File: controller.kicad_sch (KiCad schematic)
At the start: 42 parts, among them J1 Jumper_3_Bridged12, J2 EEPROM DISABLE, J3 Conn_02x20_Odd_Even, J4 5V, J5 USB_B_Mini, J6 Conn_01x05, J7 Jumper_3_Bridged12, SW2 RST, U1 CY7C68013A-56PVX, U2 AZ1117-3.3, U3 CAT24C128, Y1 24MHz

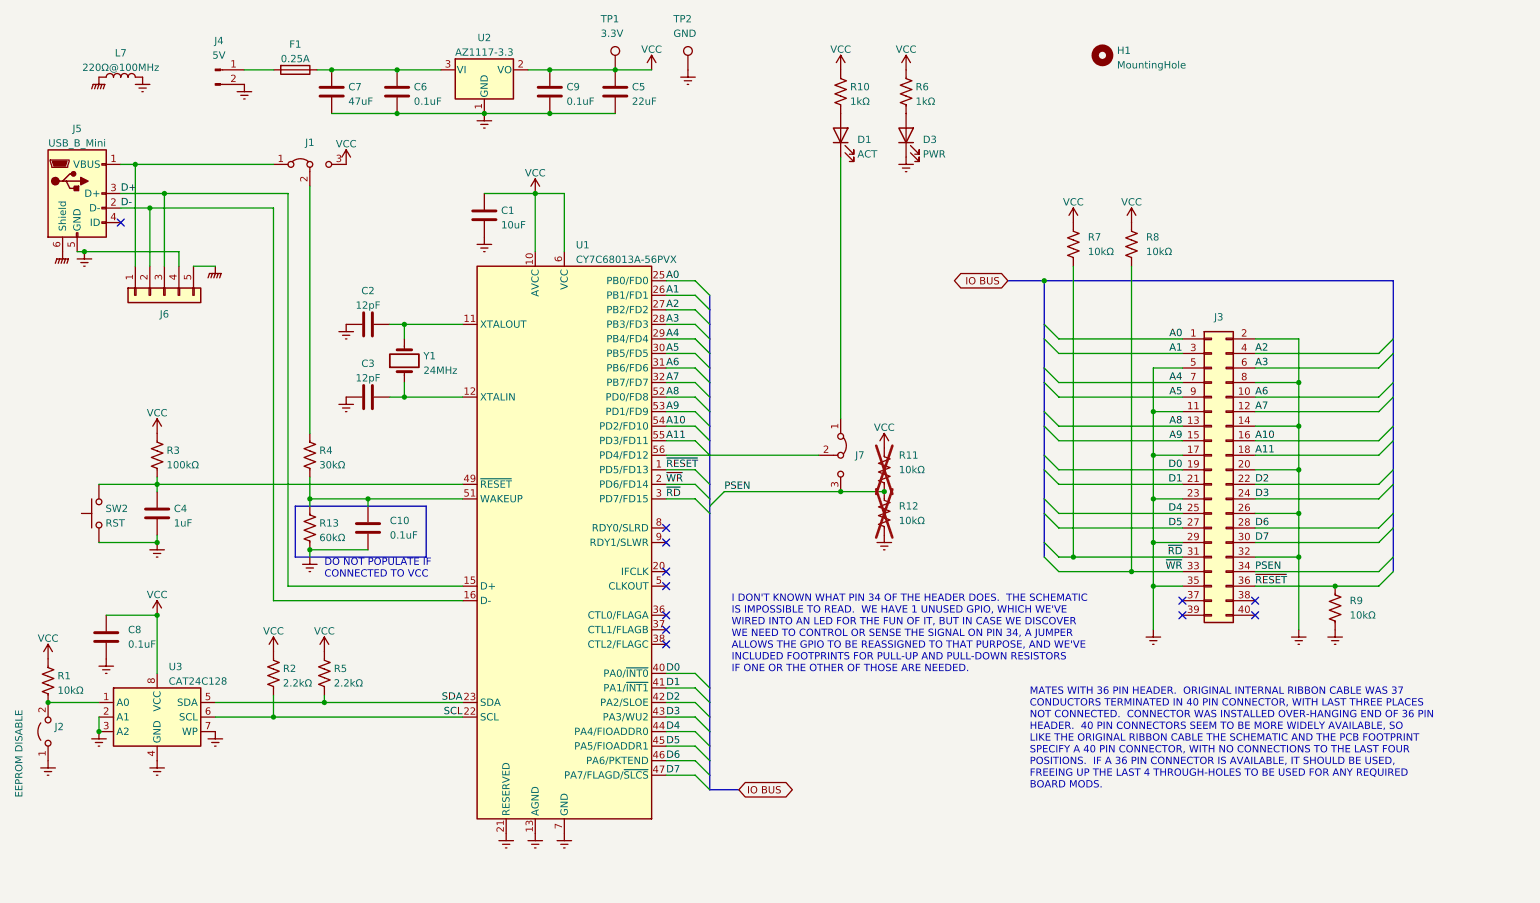
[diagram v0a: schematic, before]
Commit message: let's call this "version 2"
- this is a cleaned-up version of the board that was built and installed in the programmer
- the WAKEUP drain resistor & timing capacitor are included
- the board is hard-wired into the self-powered configuration (USB VBUS only used for WAKEUP)
- power delivery to the FX2 chip is (probably) improved
- the ground plane has fewer interruptions
- (almost) all spare pads and through-holes to accommodate possible mistakes are removed because they're known to not be needed
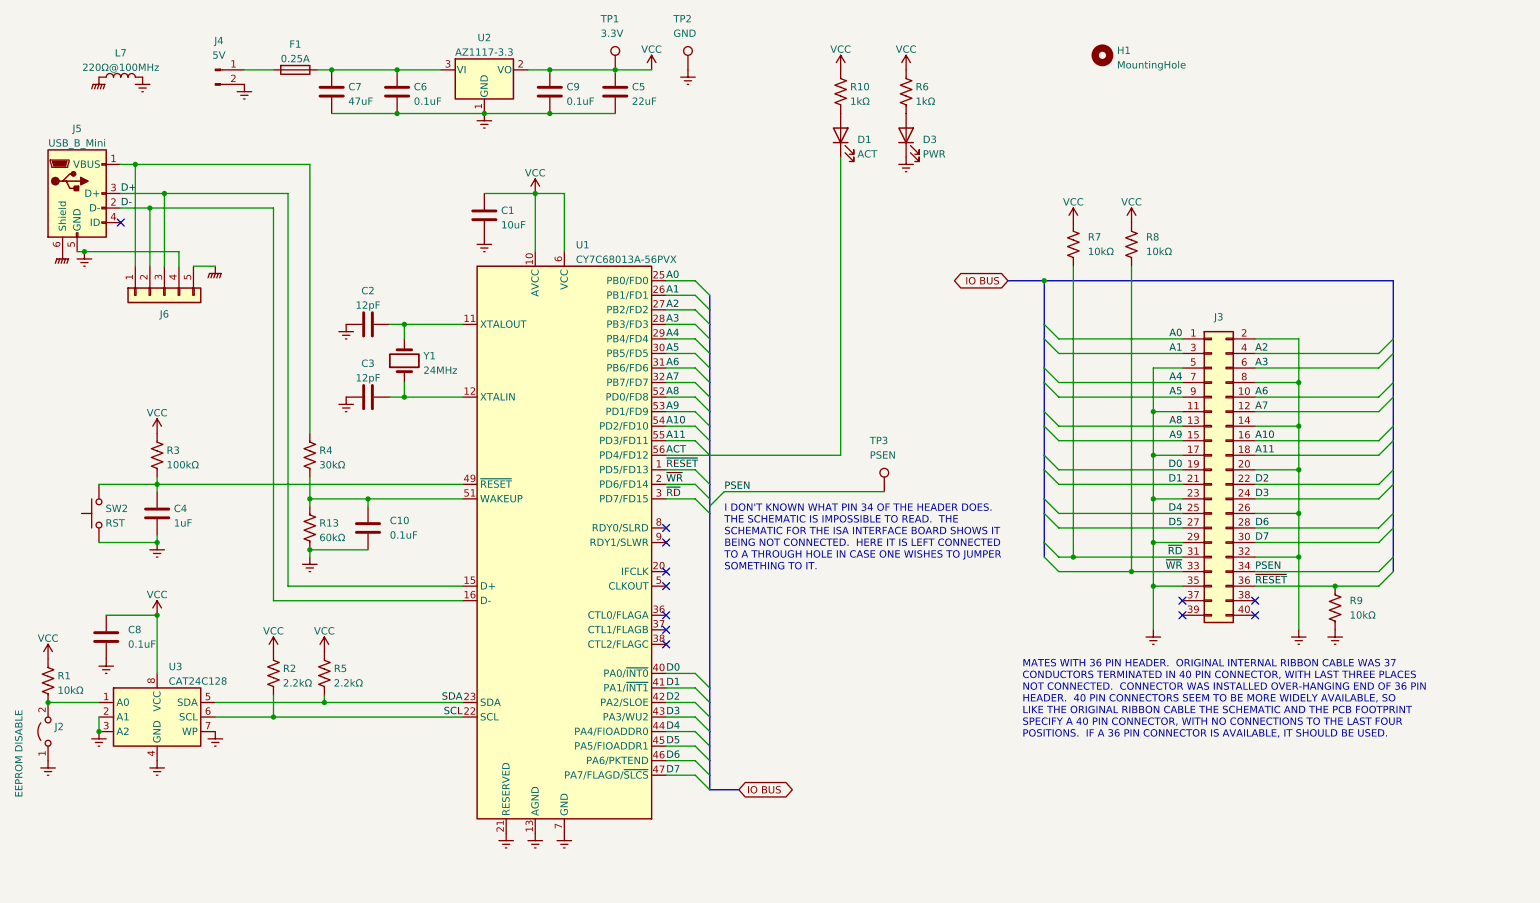
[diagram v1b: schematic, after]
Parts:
- removed J1, J7: Jumper_3_Bridged12, Jumper:SolderJumper-3_P2.0mm_Open_TrianglePad1.0x1.5mm, symbol Jumper:Jumper_3_Bridged12
- removed R11, R12: 10kΩ, Resistor_SMD:R_0805_2012Metric_Pad1.20x1.40mm_HandSolder, symbol Device:R_US
- added TP3: PSEN, TestPoint:TestPoint_THTPad_D2.0mm_Drill1.0mm, symbol Connector:TestPoint
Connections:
- net PSEN: now also TP3.1
- net at R4.1: now also J5.1 (VBUS), J6.1 (Pin_1)
- net ACT: now reaches D1.1 (K)
- net ACT: now also U1.56 (PD4/FD12)
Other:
- note added: "I DON'T KNOWN WHAT PIN 34 OF THE HEADER DOES. THE SCHEMATIC IS IMPOSSIBLE TO READ. THE SCHEMATIC FOR THE ISA INTERFACE BOARD SHOWS IT BEING NOT CONNECTED. HERE IT IS LEFT CONNECTED TO A THROUGH HOLE IN CASE ONE WISHES TO JUMPER SOMETHING TO IT."
- note removed: "DO NOT POPULATE IF CONNECTED TO VCC"
- note removed: "I DON'T KNOWN WHAT PIN 34 OF THE HEADER DOES. THE SCHEMATIC IS IMPOSSIBLE TO READ. WE HAVE 1 UNUSED GPIO, WHICH WE'VE WIRED INTO AN LED FOR THE FUN OF IT, BUT IN CASE WE DISCOVER WE NEED TO CONTROL OR SENSE THE SIGNAL ON PIN 34, A JUMPER ALLOWS THE GPIO TO BE REASSIGNED TO THAT PURPOSE, AND WE'VE INCLUDED FOOTPRINTS FOR PULL-UP AND PULL-DOWN RESISTORS IF ONE OR THE OTHER OF THOSE ARE NEEDED."

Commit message: minor improvements
- update to current symbols and footprints
- flip the GPIO and I2C pin headers to the back to avoid damage when the case is opened.  this just changes the silk screen, one can choose to solder them in either way regardless.
- kicad now offers a better crystal footprint.  switch to it so the holes are more appropriately sized
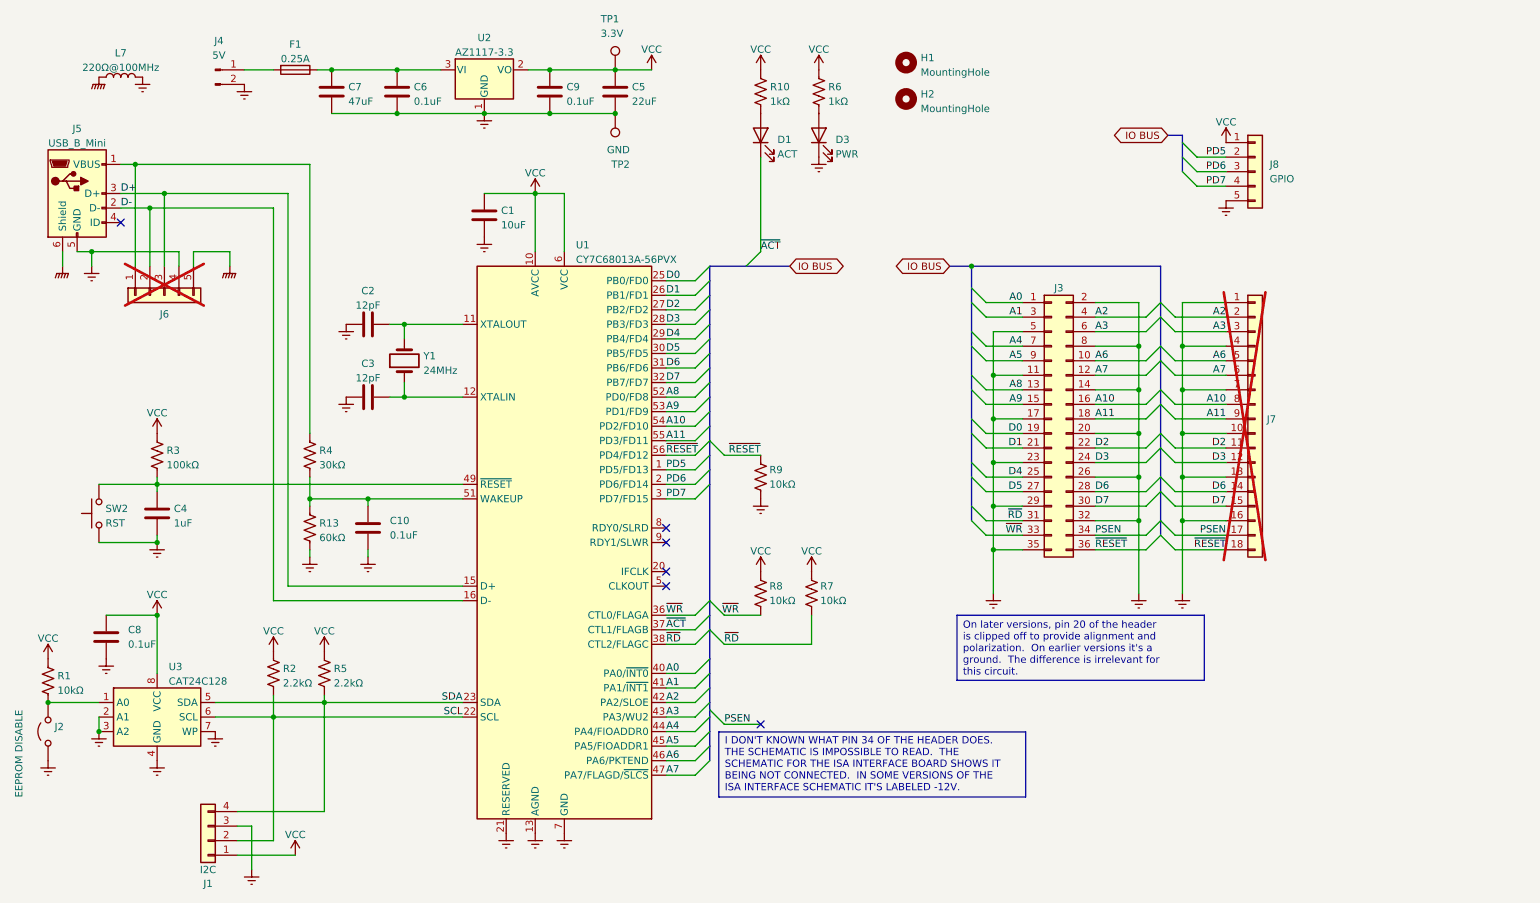
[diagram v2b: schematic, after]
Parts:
- removed J3: Conn_02x20_Odd_Even, Connector_PinSocket_2.54mm:PinSocket_2x20_P2.54mm_Horizontal, symbol Connector_Generic:Conn_02x20_Odd_Even
- removed TP3: PSEN, TestPoint:TestPoint_THTPad_D2.0mm_Drill1.0mm, symbol Connector:TestPoint
- added H2: MountingHole, MountingHole:MountingHole_3.2mm_M3, symbol Mechanical:MountingHole
- added J1: I2C, Connector_PinHeader_1.27mm:PinHeader_1x04_P1.27mm_Vertical, symbol Connector_Generic:Conn_01x04
- added J3: Conn_02x18_Odd_Even, Connector_PinSocket_2.54mm:PinSocket_2x18_P2.54mm_Horizontal, symbol Connector_Generic:Conn_02x18_Odd_Even
- added J7: Conn_01x18, Connector_PinSocket_2.54mm:PinSocket_1x18_P2.54mm_Vertical, symbol Connector_Generic:Conn_01x18
- added J8: GPIO, Connector_PinHeader_1.27mm:PinHeader_1x05_P1.27mm_Vertical, symbol Connector_Generic:Conn_01x05
- H1, TP1, TP2: now left out of the parts list
- J4: footprint Connector_Molex:Molex_Micro-Fit_3.0_43045-0212_2x01_P3.00mm_Vertical -> Connector_TE-Connectivity:TE_440054-2_1x02_P2.00mm_Vertical
- J6: now not fitted
- Y1: footprint Crystal:Crystal_HC50_Vertical -> Crystal:Crystal_HC49-4H_Vertical
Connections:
- net A0: now also U1.40 (PA0/~{INT0}), J3.1 (Pin_1); no longer U1.25 (PB0/FD0)
- net A1: now also U1.41 (PA1/~{INT1}), J3.3 (Pin_3); no longer U1.26 (PB1/FD1)
- net A10: now also J3.16 (Pin_16), J7.8 (Pin_8)
- net A11: now also J3.18 (Pin_18), J7.9 (Pin_9)
- net A2: now also U1.42 (PA2/SLOE), J3.4 (Pin_4), J7.2 (Pin_2); no longer U1.27 (PB2/FD2)
- net A3: now also U1.43 (PA3/WU2), J3.6 (Pin_6), J7.3 (Pin_3); no longer U1.28 (PB3/FD3)
- net A4: now also U1.44 (PA4/FIOADDR0), J3.7 (Pin_7); no longer U1.29 (PB4/FD4)
- net A5: now also U1.45 (PA5/FIOADDR1), J3.9 (Pin_9); no longer U1.30 (PB5/FD5)
- net A6: now also U1.46 (PA6/PKTEND), J3.10 (Pin_10), J7.5 (Pin_5); no longer U1.31 (PB6/FD6)
- net A7: now also U1.47 (PA7/FLAGD/~{SLCS}), J3.12 (Pin_12), J7.6 (Pin_6); no longer U1.32 (PB7/FD7)
- net A8: now also J3.13 (Pin_13)
- net A9: now also J3.15 (Pin_15)
- net D0: now also U1.25 (PB0/FD0), J3.19 (Pin_19); no longer U1.40 (PA0/~{INT0})
- net D1: now also U1.26 (PB1/FD1), J3.21 (Pin_21); no longer U1.41 (PA1/~{INT1})
- net D2: now also U1.27 (PB2/FD2), J3.22 (Pin_22), J7.11 (Pin_11); no longer U1.42 (PA2/SLOE)
- net D3: now also U1.28 (PB3/FD3), J3.24 (Pin_24), J7.12 (Pin_12); no longer U1.43 (PA3/WU2)
- net D4: now also U1.29 (PB4/FD4), J3.25 (Pin_25); no longer U1.44 (PA4/FIOADDR0)
- net D5: now also U1.30 (PB5/FD5), J3.27 (Pin_27); no longer U1.45 (PA5/FIOADDR1)
- net D6: now also U1.31 (PB6/FD6), J3.28 (Pin_28), J7.14 (Pin_14); no longer U1.46 (PA6/PKTEND)
- net D7: now also U1.32 (PB7/FD7), J3.30 (Pin_30), J7.15 (Pin_15); no longer U1.47 (PA7/FLAGD/~{SLCS})
- net GNDREF: now also J1.3 (Pin_3), J3.11 (Pin_11), J3.14 (Pin_14), J3.17 (Pin_17), J3.2 (Pin_2), J3.20 (Pin_20), J3.23 (Pin_23), J3.26 (Pin_26), J3.29 (Pin_29), J3.32 (Pin_32), J3.35 (Pin_35), J3.5 (Pin_5), J3.8 (Pin_8), J7.1 (Pin_1), J7.10 (Pin_10), J7.13 (Pin_13), J7.16 (Pin_16), J7.4 (Pin_4), J7.7 (Pin_7), J8.5 (Pin_5)
- net PSEN: now also J3.34 (Pin_34), J7.17 (Pin_17)
- net SCL: now also J1.2 (Pin_2)
- net SDA: now also J1.4 (Pin_4)
- net VCC: now also J1.1 (Pin_1), J8.1 (Pin_1)
- net ~{RD}: now also U1.38 (CTL2/FLAGC), J3.31 (Pin_31); no longer U1.3 (PD7/FD15)
- net ~{RESET}: now also U1.56 (PD4/FD12), J3.36 (Pin_36), J7.18 (Pin_18); no longer U1.1 (PD5/FD13)
- net ~{WR}: now also U1.36 (CTL0/FLAGA), J3.33 (Pin_33); no longer U1.2 (PD6/FD14)
- net ~{ACT}: now reaches U1.37 (CTL1/FLAGB)
- net ~{ACT}: now also D1.1 (K)
- removed net ACT: D1.1 (K), U1.56 (PD4/FD12)
- new net PD5: J8.2 (Pin_2), U1.1 (PD5/FD13)
- new net PD6: J8.3 (Pin_3), U1.2 (PD6/FD14)
- new net PD7: J8.4 (Pin_4), U1.3 (PD7/FD15)
- no-connect marks 12 -> 6
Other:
- note removed: "I DON'T KNOWN WHAT PIN 34 OF THE HEADER DOES. THE SCHEMATIC IS IMPOSSIBLE TO READ. THE SCHEMATIC FOR THE ISA INTERFACE BOARD SHOWS IT BEING NOT CONNECTED. HERE IT IS LEFT CONNECTED TO A THROUGH HOLE IN CASE ONE WISHES TO JUMPER SOMETHING TO IT."
- note removed: "MATES WITH 36 PIN HEADER. ORIGINAL INTERNAL RIBBON CABLE WAS 37 CONDUCTORS TERMINATED IN 40 PIN CONNECTOR, WITH LAST THREE PLACES NOT CONNECTED. CONNECTOR WAS INSTALLED OVER-HANGING END OF 36 PIN HEADER. 40 PIN CONNECTORS SEEM TO BE MORE WIDELY AVAILABLE, SO LIKE THE ORIGINAL RIBBON CABLE THE SCHEMATIC AND THE PCB FOOTPRINT SPECIFY A 40 PIN CONNECTOR, WITH NO CONNECTIONS TO THE LAST FOUR POSITION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"
- moved on the sheet: D1, D3, H1, R10, R6, TP2
